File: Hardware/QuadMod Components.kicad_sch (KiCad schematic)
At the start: 118 parts, among them J1 Conn_01x08_Pin, J2 Conn_01x08_Pin, J3 Conn_01x08_Pin, J4 Conn_01x08_Pin, J5 Eurorack_10_pin_power, J7 Prog_Header, J7 USB_B_Micro, J8 Extra_Outs, U1 STF202-22T1G, U2 STM32H563VIT, U3 TL072, U4 MCP6004, U6 TPS561201, U7 LD1117-3.3-4Tab, U7 MCP6002-xSN, U9 AK4619VN, Y1 8MHz 20pF

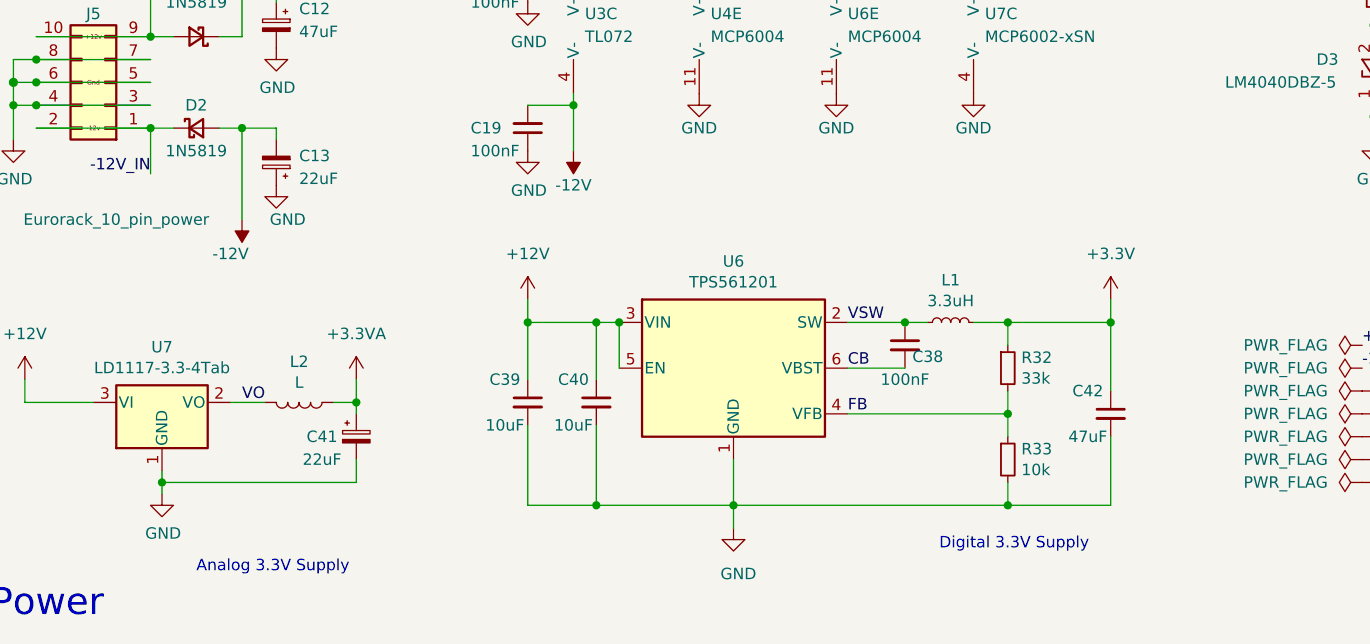
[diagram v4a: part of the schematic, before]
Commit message: First draft of power routing completed
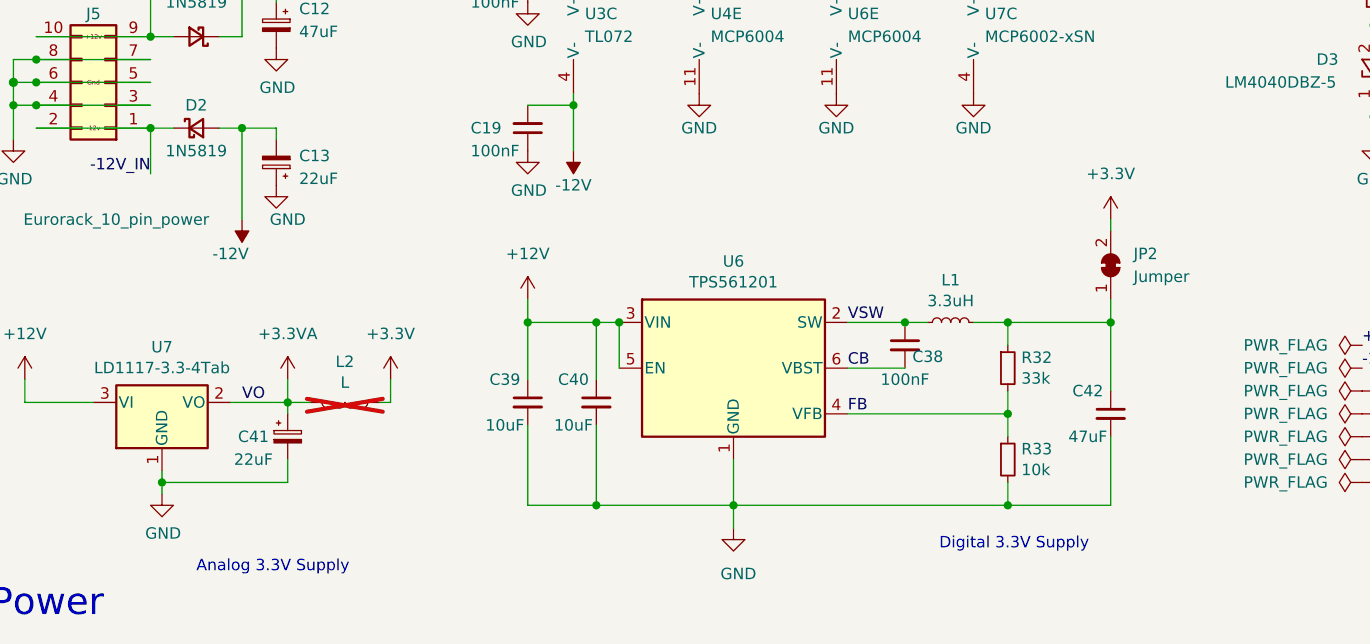
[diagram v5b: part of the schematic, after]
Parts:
- added JP2: Jumper, Jumper:SolderJumper-2_P1.3mm_Bridged2Bar_RoundedPad1.0x1.5mm, symbol Jumper:SolderJumper_2_Bridged
- L2: now not fitted; now left out of the parts list
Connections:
- net VO is gone; now on net +3.3VA: L2.2, U7.2 (VO)
- net +3.3V: now also L2.1, JP2.2 (B); no longer C42.1, L1.2, R32.1
- net +3.3VA: no longer L2.1
- new net: C42.1, JP2.1 (A), L1.2, R32.1
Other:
- moved on the sheet: C41
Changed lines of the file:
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@@
   (junction (at 78.74 245.11) (diameter 0) (color 0 0 0 0)
   )
-  (junction (at 59.69 254) (diameter 0) (color 0 0 0 0)
+  (junction (at 52.07 254) (diameter 0) (color 0 0 0 0)
   )
   (junction (at 300.99 142.24) (diameter 0) (color 0 0 0 0)
@@
     (stroke (width 0) (type default))
   )
+  (wire (pts (xy 63.5 254) (xy 62.23 254))
+    (stroke (width 0) (type default))
+  )
   (wire (pts (xy 364.49 78.74) (xy 364.49 76.2))
     (stroke (width 0) (type default))
@@
     (stroke (width 0) (type default))
   )
-  (wire (pts (xy 59.69 254) (xy 57.15 254))
+  (wire (pts (xy 45.72 254) (xy 52.07 254))
     (stroke (width 0) (type default))
   )
@@
     (stroke (width 0) (type default))
   )
-  (wire (pts (xy 45.72 254) (xy 49.53 254))
-    (stroke (width 0) (type default))
-  )
   (wire (pts (xy 21.59 220.98) (xy 24.13 220.98))
     (stroke (width 0) (type solid))
@@
     (stroke (width 0) (type default))
   )
+  (wire (pts (xy 63.5 251.46) (xy 63.5 254))
+    (stroke (width 0) (type default))
+  )
   (wire (pts (xy 243.84 30.48) (xy 247.65 30.48))
     (stroke (width 0) (type default))
   )
-  (wire (pts (xy 59.69 255.27) (xy 59.69 254))
+  (wire (pts (xy 52.07 255.27) (xy 52.07 254))
     (stroke (width 0) (type default))
   )
@@
     (stroke (width 0) (type default))
   )
-  (wire (pts (xy 59.69 260.35) (xy 59.69 262.89))
+  (wire (pts (xy 52.07 260.35) (xy 52.07 262.89))
     (stroke (width 0) (type default))
   )
@@
     (stroke (width 0) (type default))
   )
-  (wire (pts (xy 59.69 251.46) (xy 59.69 254))
+  (wire (pts (xy 52.07 251.46) (xy 52.07 254))
     (stroke (width 0) (type default))
   )
@@
     (stroke (width 0) (type default))
   )
-  (wire (pts (xy 38.1 262.89) (xy 59.69 262.89))
+  (wire (pts (xy 38.1 262.89) (xy 52.07 262.89))
     (stroke (width 0) (type default))
   )
@@
     (stroke (width 0) (type default))
   )
+  (wire (pts (xy 52.07 254) (xy 54.61 254))
+    (stroke (width 0) (type default))
+  )
   (wire (pts (xy 300.99 172.72) (xy 300.99 179.07))
     (stroke (width 0) (type default))
@@
     (stroke (width 0) (type default))
   )
+  (wire (pts (xy 143.51 233.68) (xy 143.51 234.95))
+    (stroke (width 0) (type default))
+  )
   (wire (pts (xy 175.26 30.48) (xy 170.18 30.48))
     (stroke (width 0) (type default))
@@
     )
   )
-  (symbol (lib_id "power:+3.3VA") (at 59.69 251.46 0) (unit 1)
+  (symbol (lib_id "power:+3.3VA") (at 52.07 251.46 0) (unit 1)
     (in_bom yes) (on_board yes) (dnp no) (fields_autoplaced)
-    (property "Reference" "#PWR068" (at 59.69 255.27 0)
+    (property "Reference" "#PWR068" (at 52.07 255.27 0)
       (effects (font (size 1.27 1.27)) hide)
     )
-    (property "Value" "+3.3VA" (at 59.69 246.38 0)
+    (property "Value" "+3.3VA" (at 52.07 246.38 0)
       (effects (font (size 1.27 1.27)))
     )
-    (property "Footprint" "" (at 59.69 251.46 0)
+    (property "Footprint" "" (at 52.07 251.46 0)
       (effects (font (size 1.27 1.27)) hide)
     )
-    (property "Datasheet" "" (at 59.69 251.46 0)
+    (property "Datasheet" "" (at 52.07 251.46 0)
       (effects (font (size 1.27 1.27)) hide)
     )
@@
     )
   )
+  (symbol (lib_id "Jumper:SolderJumper_2_Bridged") (at 143.51 238.76 90) (unit 1)
+    (in_bom yes) (on_board yes) (dnp no) (fields_autoplaced)
+    (property "Reference" "JP2" (at 146.05 237.49 90)
+      (effects (font (size 1.27 1.27)) (justify right))
+    )
+    (property "Value" "Jumper" (at 146.05 240.03 90)
+      (effects (font (size 1.27 1.27)) (justify right))
+    )
+    (property "Footprint" "Jumper:SolderJumper-2_P1.3mm_Bridged2Bar_RoundedPad1.0x1.5mm" (at 143.51 238.76 0)
+      (effects (font (size 1.27 1.27)) hide)
+    )
+    (property "Datasheet" "~" (at 143.51 238.76 0)
+      (effects (font (size 1.27 1.27)) hide)
+    )
+    (pin "2")
+    (pin "1")
+    (instances
+      (project "QuadMod Components"
+        (path "/d7d98a4b-a059-4480-8e77-1d52297d5f57"
+          (reference "JP2") (unit 1)
+        )
+      )
+    )
+  )
   (symbol (lib_id "power:+3.3V") (at 158.75 27.94 0) (unit 1)
     (in_bom yes) (on_board yes) (dnp no)
@@
     )
   )
+  (symbol (lib_id "power:+3.3V") (at 63.5 251.46 0) (unit 1)
+    (in_bom yes) (on_board yes) (dnp no) (fields_autoplaced)
+    (property "Reference" "#PWR063" (at 63.5 255.27 0)
+      (effects (font (size 1.27 1.27)) hide)
+    )
+    (property "Value" "+3.3V" (at 63.5 246.38 0)
+      (effects (font (size 1.27 1.27)))
+    )
+    (property "Footprint" "" (at 63.5 251.46 0)
+      (effects (font (size 1.27 1.27)) hide)
+    )
+    (property "Datasheet" "" (at 63.5 251.46 0)
+      (effects (font (size 1.27 1.27)) hide)
+    )
+    (pin "1")
+    (instances
+      (project "Punck_Components"
+        (path "/863a2fa5-cc81-43c1-8f46-cd3e70a7a26b"
+          (reference "#PWR063") (unit 1)
+        )
+      )
+      (project "QuadMod Components"
+        (path "/d7d98a4b-a059-4480-8e77-1d52297d5f57"
+          (reference "#PWR073") (unit 1)
+        )
+      )
+    )
+  )
   (symbol (lib_id "Device:R") (at 295.91 33.02 270) (unit 1)
     (in_bom yes) (on_board yes) (dnp no)
@@
     )
   )
-  (symbol (lib_id "Device:C_Polarized_Small") (at 59.69 257.81 0) (unit 1)
+  (symbol (lib_id "Device:C_Polarized_Small") (at 52.07 257.81 0) (unit 1)
     (in_bom yes) (on_board yes) (dnp no)
-    (property "Reference" "C41" (at 55.88 257.81 0)
+    (property "Reference" "C41" (at 48.26 257.81 0)
       (effects (font (size 1.27 1.27)))
     )
-    (property "Value" "22uF" (at 55.88 260.35 0)
+    (property "Value" "22uF" (at 48.26 260.35 0)
       (effects (font (size 1.27 1.27)))
     )
-    (property "Footprint" "Capacitor_SMD:CP_Elec_4x5.8" (at 59.69 257.81 0)
+    (property "Footprint" "Capacitor_SMD:CP_Elec_4x5.8" (at 52.07 257.81 0)
       (effects (font (size 1.27 1.27)) hide)
     )
-    (property "Datasheet" "~" (at 59.69 257.81 0)
+    (property "Datasheet" "~" (at 52.07 257.81 0)
       (effects (font (size 1.27 1.27)) hide)
     )
-    (property "Part_Number" "C134793" (at 59.69 257.81 0)
+    (property "Part_Number" "C134793" (at 52.07 257.81 0)
       (effects (font (size 1.27 1.27)) hide)
     )
-    (property "Rotation" "180" (at 59.69 257.81 0)
+    (property "Rotation" "180" (at 52.07 257.81 0)
       (effects (font (size 1.27 1.27)) hide)
     )
@@
     )
   )
-  (symbol (lib_id "Device:L") (at 53.34 254 270) (unit 1)
-    (in_bom yes) (on_board yes) (dnp no)
-    (property "Reference" "L2" (at 53.34 249.4788 90)
+  (symbol (lib_id "Device:L") (at 58.42 254 270) (unit 1)
+    (in_bom no) (on_board yes) (dnp yes)
+    (property "Reference" "L2" (at 58.42 249.4788 90)
       (effects (font (size 1.27 1.27)))
     )
-    (property "Value" "L" (at 53.34 251.7902 90)
+    (property "Value" "L" (at 58.42 251.7902 90)
       (effects (font (size 1.27 1.27)))
     )
-    (property "Footprint" "Inductor_SMD:L_0805_2012Metric" (at 53.34 254 0)
+    (property "Footprint" "Inductor_SMD:L_0805_2012Metric" (at 58.42 254 0)
       (effects (font (size 1.27 1.27)) hide)
     )
-    (property "Datasheet" "~" (at 53.34 254 0)
+    (property "Datasheet" "~" (at 58.42 254 0)
       (effects (font (size 1.27 1.27)) hide)
     )
-    (property "Part_Number" "C1046" (at 53.34 254 0)
+    (property "Part_Number" "C1046" (at 58.42 254 0)
       (effects (font (size 1.27 1.27)) hide)
     )
@@
     )
   )
-  (symbol (lib_id "power:+3.3V") (at 143.51 242.57 0) (unit 1)
+  (symbol (lib_id "power:+3.3V") (at 143.51 233.68 0) (unit 1)
     (in_bom yes) (on_board yes) (dnp no) (fields_autoplaced)
-    (property "Reference" "#PWR063" (at 143.51 246.38 0)
+    (property "Reference" "#PWR063" (at 143.51 237.49 0)
       (effects (font (size 1.27 1.27)) hide)
     )
-    (property "Value" "+3.3V" (at 143.51 237.49 0)
+    (property "Value" "+3.3V" (at 143.51 228.6 0)
       (effects (font (size 1.27 1.27)))
     )
-    (property "Footprint" "" (at 143.51 242.57 0)
+    (property "Footprint" "" (at 143.51 233.68 0)
       (effects (font (size 1.27 1.27)) hide)
     )
-    (property "Datasheet" "" (at 143.51 242.57 0)
+    (property "Datasheet" "" (at 143.51 233.68 0)
       (effects (font (size 1.27 1.27)) hide)
     )

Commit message: Basic layout complete
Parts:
- JP2: footprint Jumper:SolderJumper-2_P1.3mm_Bridged2Bar_RoundedPad1.0x1.5mm -> Jumper:SolderJumper-2_P1.3mm_Open_RoundedPad1.0x1.5mm
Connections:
- net D3V3: now reaches C42.1, JP2.1 (A), L1.2, R32.1
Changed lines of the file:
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@@
+    (effects (font (size 1.27 1.27)) (justify left bottom))
+  )
+  (label "D3V3" (at 132.08 245.11 0) (fields_autoplaced)
     (effects (font (size 1.27 1.27)) (justify left bottom))
   )
@@
       (effects (font (size 1.27 1.27)) (justify right))
     )
-    (property "Footprint" "Jumper:SolderJumper-2_P1.3mm_Bridged2Bar_RoundedPad1.0x1.5mm" (at 143.51 238.76 0)
-      (effects (font (size 1.27 1.27)) hide)
-    )
+    (property "Footprint" "Jumper:SolderJumper-2_P1.3mm_Open_RoundedPad1.0x1.5mm" (at 143.51 238.76 0)
+      (effects (font (size 1.27 1.27)) hide)
+    )

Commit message: First draft of control board
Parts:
- removed R7: 47k, Resistor_SMD:R_0603_1608Metric_Pad0.98x0.95mm_HandSolder, symbol Device:R
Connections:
- net CLOCK is gone; now on net DLY_TIME_CV: J1.7 (Pin_7), U7.5 (+)
- net +3.3VA: now also J4.3 (Pin_3); no longer J4.7 (Pin_7)
- net DLY_FEEDBACK: now also J3.2 (Pin_2), U2.25 (PA2); no longer J4.1 (Pin_1), U2.31 (PA6)
- net DLY_TIME_CV: now also R5.2; no longer J1.1 (Pin_1), R5.2
- net DLY_TIME_POT: now also J1.6 (Pin_6), U2.16 (PC1); no longer J1.2 (Pin_2), R7.2
- net Delay_Time: now also R6.1, U2.24 (PA1), U7.1; no longer R6.1, U2.35 (PB0), U3.7
- net GND: now also J1.5 (Pin_5), J4.7 (Pin_7)
- net LFO_BASEFREQ_CV: now also J1.1 (Pin_1), R5.2; no longer J1.5 (Pin_5), R5.2
- net LFO_BASEFREQ_POT: now also J1.2 (Pin_2), R7.2; no longer J1.6 (Pin_6)
- net LFO_Base_Freq: now also R6.1, U2.35 (PB0), U3.7; no longer R6.1, U2.24 (PA1), U7.1
- net LFO_RANGE: now also J4.1 (Pin_1), U2.31 (PA6); no longer J3.2 (Pin_2), U2.25 (PA2)
- no-connect marks 52 -> 51
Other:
- note added: "Autodetect whether Delay time input is a clock or a CV"
- moved on the sheet: R1, R5, R6, U7A, U7B

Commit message: Started adding additional clock LED
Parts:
- added R17: 1k, Resistor_SMD:R_0603_1608Metric_Pad0.98x0.95mm_HandSolder, symbol Device:R_Small
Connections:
- net +3.3VA: now also J3.8 (Pin_8); no longer J2.1 (Pin_1), J3.7 (Pin_7)
- net DELAY_LED: now also J2.7 (Pin_7); no longer J2.6 (Pin_6)
- net DLY_FILTER_CV: now also J1.4 (Pin_4); no longer J1.3 (Pin_3)
- net DLY_FILTER_POT: now also J1.5 (Pin_5); no longer J1.4 (Pin_4)
- net FX_LED: now also J2.8 (Pin_8); no longer J2.7 (Pin_7)
- net GND: now also J1.1 (Pin_1), J2.1 (Pin_1), J3.3 (Pin_3); no longer J1.5 (Pin_5), J2.8 (Pin_8), J3.8 (Pin_8)
- net IN1: now also J3.7 (Pin_7); no longer J3.6 (Pin_6)
- net IN2: now also J3.6 (Pin_6); no longer J3.5 (Pin_5)
- net IN3: now also J3.5 (Pin_5); no longer J3.4 (Pin_4)
- net IN4: now also J3.4 (Pin_4); no longer J3.3 (Pin_3)
- net LFO_BASEFREQ_CV: now also J1.2 (Pin_2); no longer J1.1 (Pin_1)
- net LFO_BASEFREQ_POT: now also J1.3 (Pin_3); no longer J1.2 (Pin_2)
- net Clocked_Led_Out: now reaches U2.61 (PD14)
- net Clocked_Led_Out: now also R17.1
- new net CLOCKED_LED: J2.6 (Pin_6), R17.2
- no-connect marks 51 -> 50
